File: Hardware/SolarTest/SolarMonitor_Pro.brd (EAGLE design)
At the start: 61 x 38.1 mm, 29 parts, among them J6 5.5x2.1mm Barrel, J8 CONN_42.54_SCREW

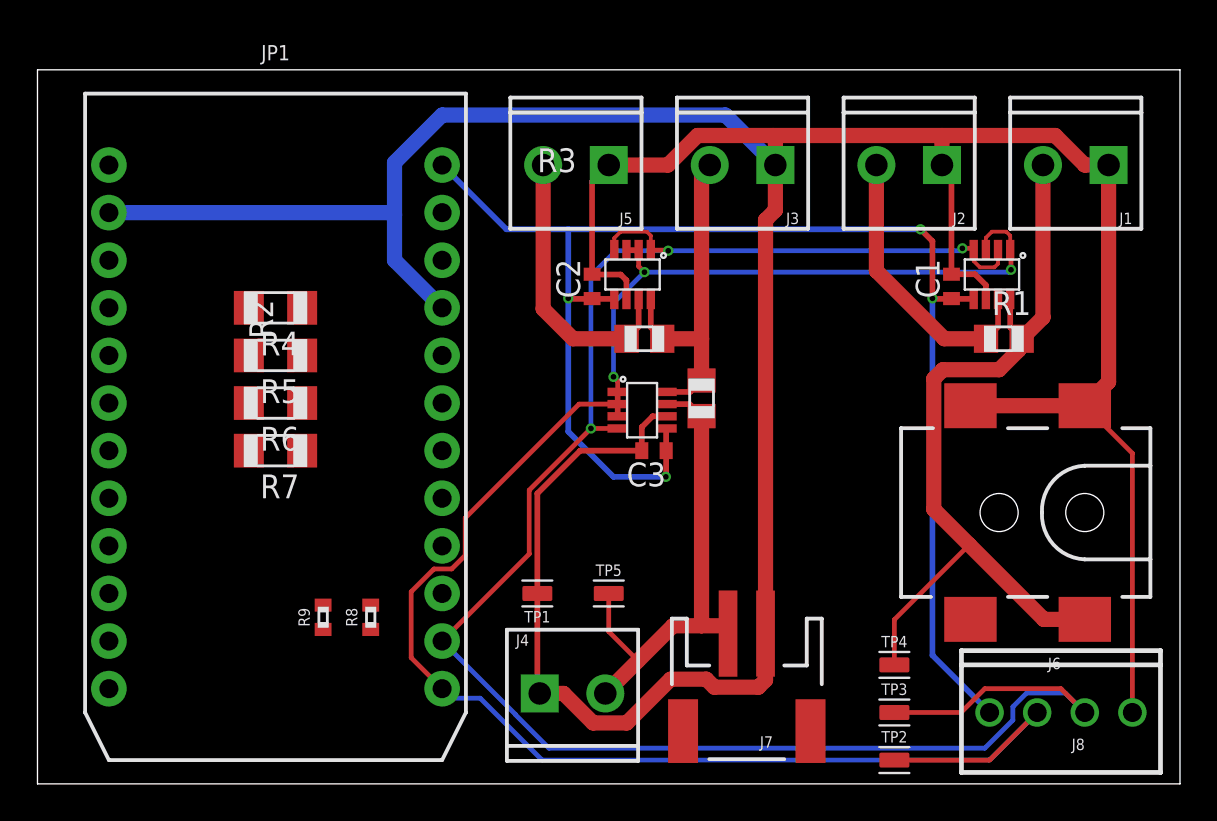
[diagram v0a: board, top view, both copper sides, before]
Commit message: Updated solar monitor board, v0 ready for fab
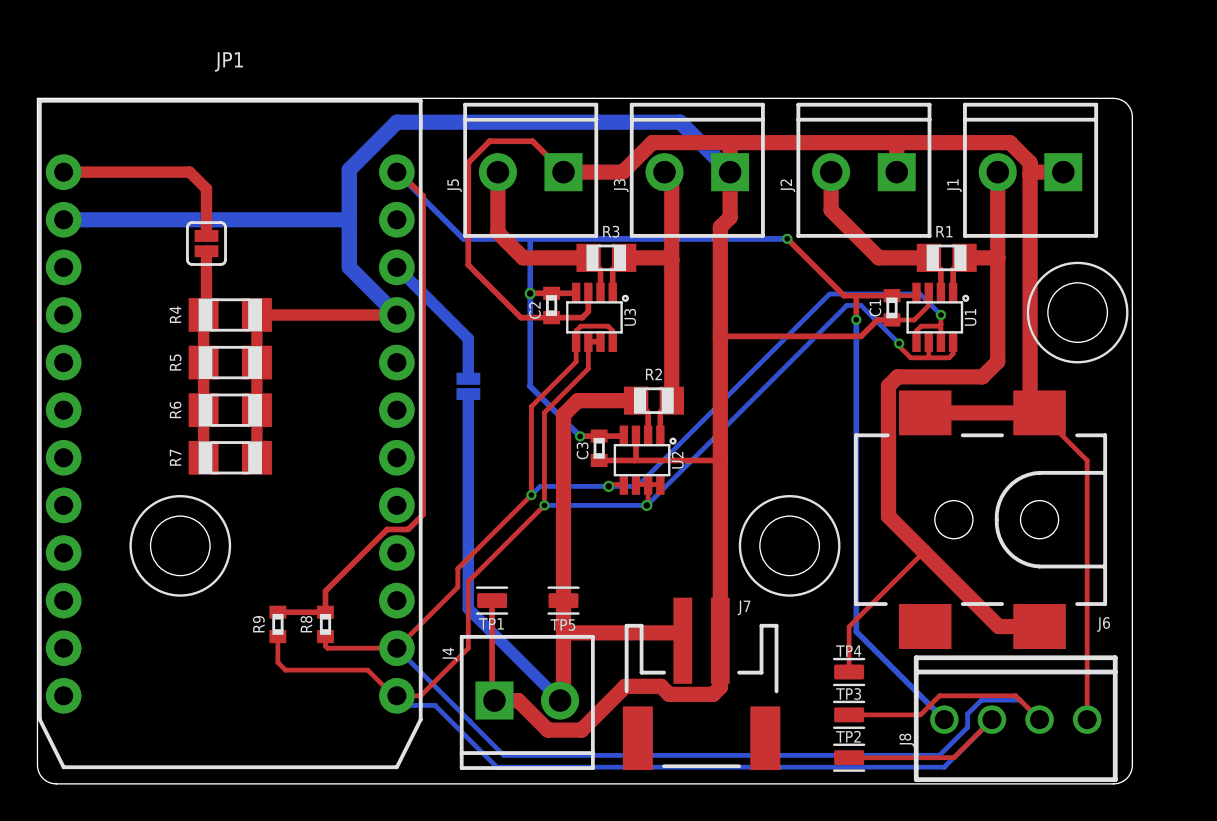
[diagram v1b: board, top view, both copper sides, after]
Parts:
- removed U$2, U$3, U$4: INA219DCN, bschulz:DCN_R-PDSO-G8
- added H1, H2, H3: (no value), bschulz:4_40
- added JP2, JP3: JUMPER-SMT_2_NC_PASTE_SILK, SparkFun-Jumpers:SMT-JUMPER_2_NC_PASTE_SILK
- added U1, U2, U3: INA219DCN, bschulz:DCN_R-PDSO-G8
- C1, C2, C3: device bschulz:C0402 -> bschulz_passives:C0402
- moved R1 5.29 mm to (48.5, 28.1)
- moved R3 4.77 mm to (30.4, 28.1)
- moved C1 3.37 mm to (45.6, 25.4), turned to 270 degrees
- moved C3 2.92 mm to (30.0, 17.9), turned to 270 degrees
- moved R2 2.54 mm to (32.9, 20.4), turned to 0 degrees
- moved J6 2.44 mm to (53.5, 14.1)
- moved J4 2.44 mm to (24.4, 4.45)
- moved J5 2.44 mm to (28.1, 32.6)
- moved R8 2.44 mm to (15.4, 8.51)
- moved R9 2.44 mm to (12.8, 8.51)
- moved TP1 2.44 mm to (24.3, 9.78)
- moved TP5 2.44 mm to (28.1, 9.78)
- moved JP1 2.44 mm to (10.3, 18.7)
- moved R4 2.44 mm to (10.3, 25.0)
- moved R5 2.44 mm to (10.3, 22.5)
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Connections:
- removed net VBAT: JP1.22
- new net FEATHER_BAT: JP1.22, JP3.2
- new net LOAD: JP2.2, R4.2, R5.2, R6.2, R7.2
- net 3V3: now also U1.4, U2.4, U3.4; no longer U$2.5, U$3.5, U$4.5
- net 5V: now also JP2.1; no longer R4.2, R5.2, R6.2, R7.2
- net BAT: now also JP3.1, U2.2; no longer U$3.7
- net GND: now also U1.3, U2.3, U3.3; no longer U$2.6, U$3.6, U$4.6
- net LOAD_OUT: now also U3.2; no longer U$4.7
- net MPPT_OUT: now also U2.1, U3.1; no longer U$3.8, U$4.8
- net PV_IN: now also U1.1; no longer U$2.8
- net PV_OUT: now also U1.2; no longer U$2.7
- net SCL: now also U1.5, U1.7, U2.5, U3.5, U3.8; no longer U$2.2, U$2.4, U$3.4, U$4.1, U$4.4
- net SDA: now also U1.6, U1.8, U2.6, U2.7, U2.8, U3.6, U3.7; no longer U$2.1, U$2.3, U$3.1, U$3.2, U$3.3, U$4.2, U$4.3
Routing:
- net GND: track 194.6 -> 218.0 mm
- net 3V3: track 78.6 -> 101.0 mm
- net BAT: track 26.0 -> 46.8 mm
- net LOAD: track 0.00 -> 11.1 mm
- net 5V: track 0.00 -> 10.5 mm
- net SDA: track 99.3 -> 107.4 mm
- net FEATHER_BAT: track 0.00 -> 7.52 mm
- net SCL: track 102.6 -> 108.9 mm
- net PV_OUT: track 15.4 -> 10.4 mm
- net LOAD_OUT: track 15.2 -> 10.8 mm
- net PV_IN: track 43.6 -> 46.6 mm
- net MPPT_OUT: track 18.3 -> 19.2 mm
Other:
- board size 61 x 38.1 mm -> 58.4 x 36.6 mm
- board text added: "+ -"
- board text added: "3v3"
- board text added: "Bat"
- board text added: "From MPPT"
- board text added: "From Solar"
- board text added: "GND"
- board text added: "J0"
- board text added: "J1"
- board text added: "PV"
- board text added: "Project LEAF Solar Power Monitor v0 Designed by Bobby Schulz 03-18-2019"
- board text added: "SCL"
- board text added: "SDA"
- board text added: "To Bat"
- board text added: "To Load"
- board text added: "To MPPT"
